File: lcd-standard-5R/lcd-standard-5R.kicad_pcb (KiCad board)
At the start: 2 copper layers, 138.2 x 93.2 mm, 56 parts, among them J1 SWD, J2 Conn_01x40_MountingPin, J3 Micro_SD_Card_Det1, J4 USB_C_Receptacle_USB2.0_16P, J5 Conn_01x06_MountingPin, SW1 BOOT0, SW2 RST, U1 siplex-som-s16, U2 TPS61169

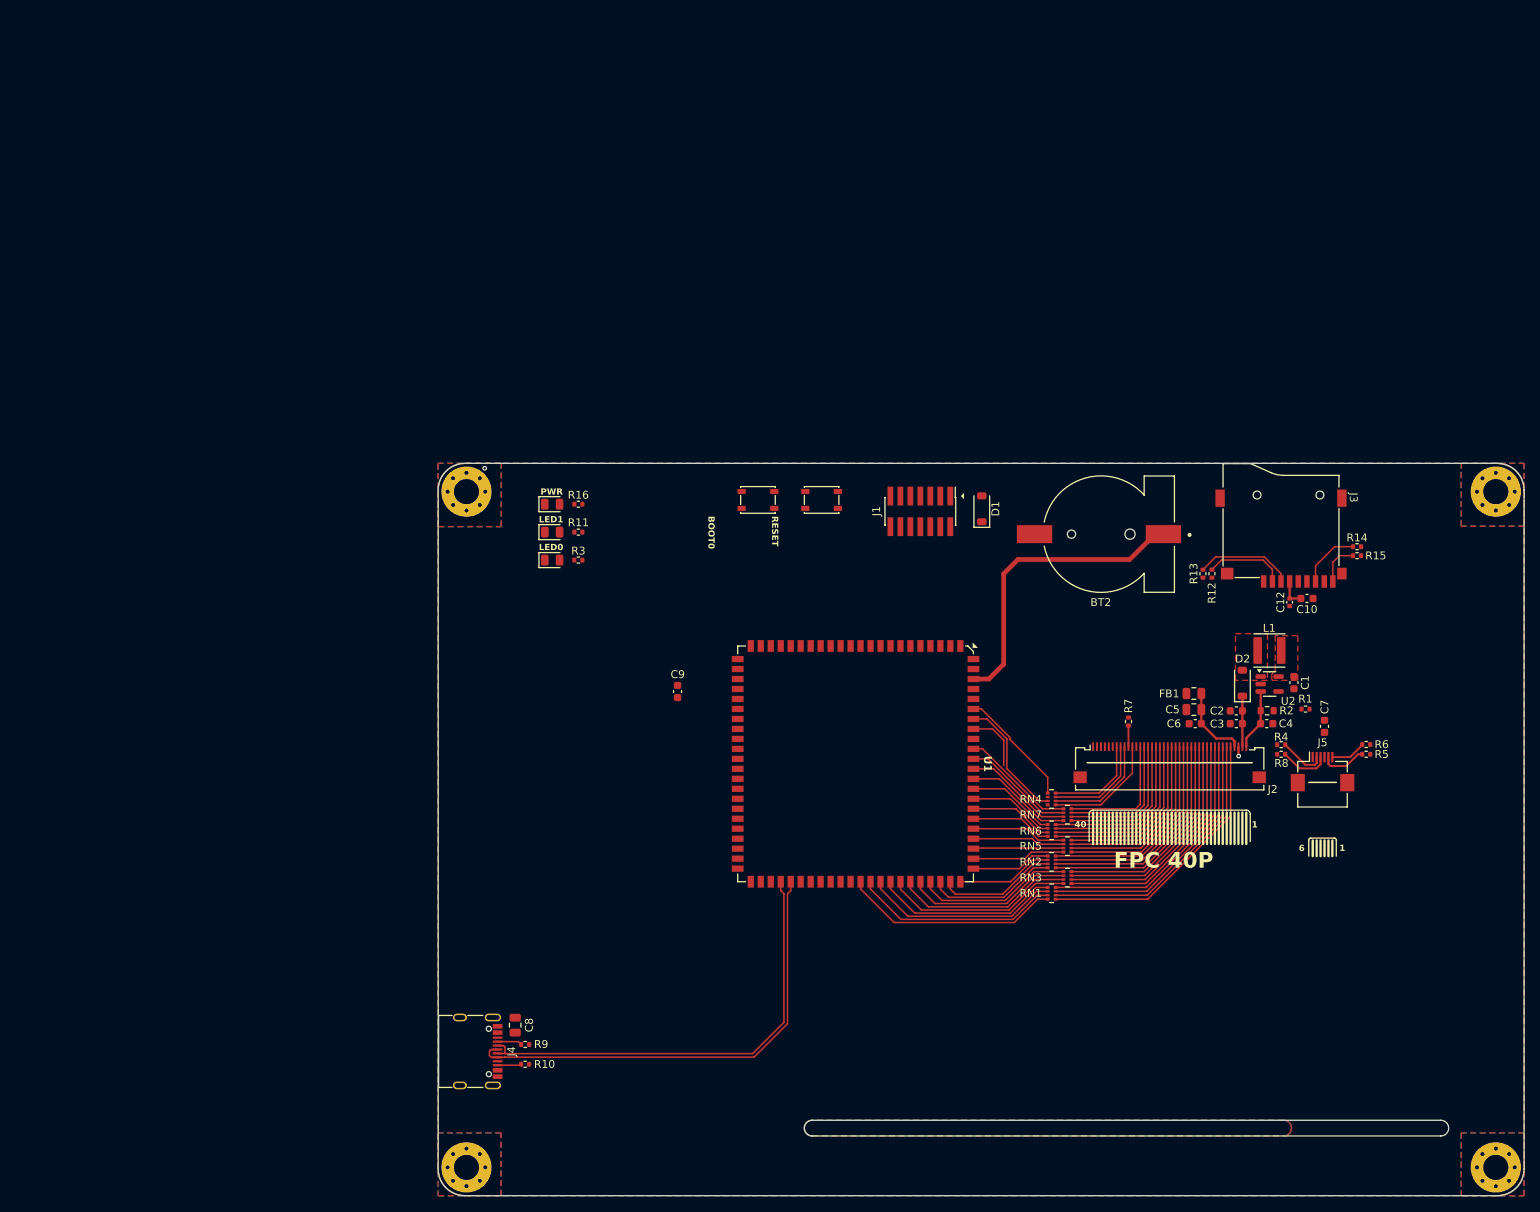
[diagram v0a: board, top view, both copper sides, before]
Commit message: Added Serial, Buzzer, AUX-IO, POWER switch, XPT2046, TAG-connect, EEPROM
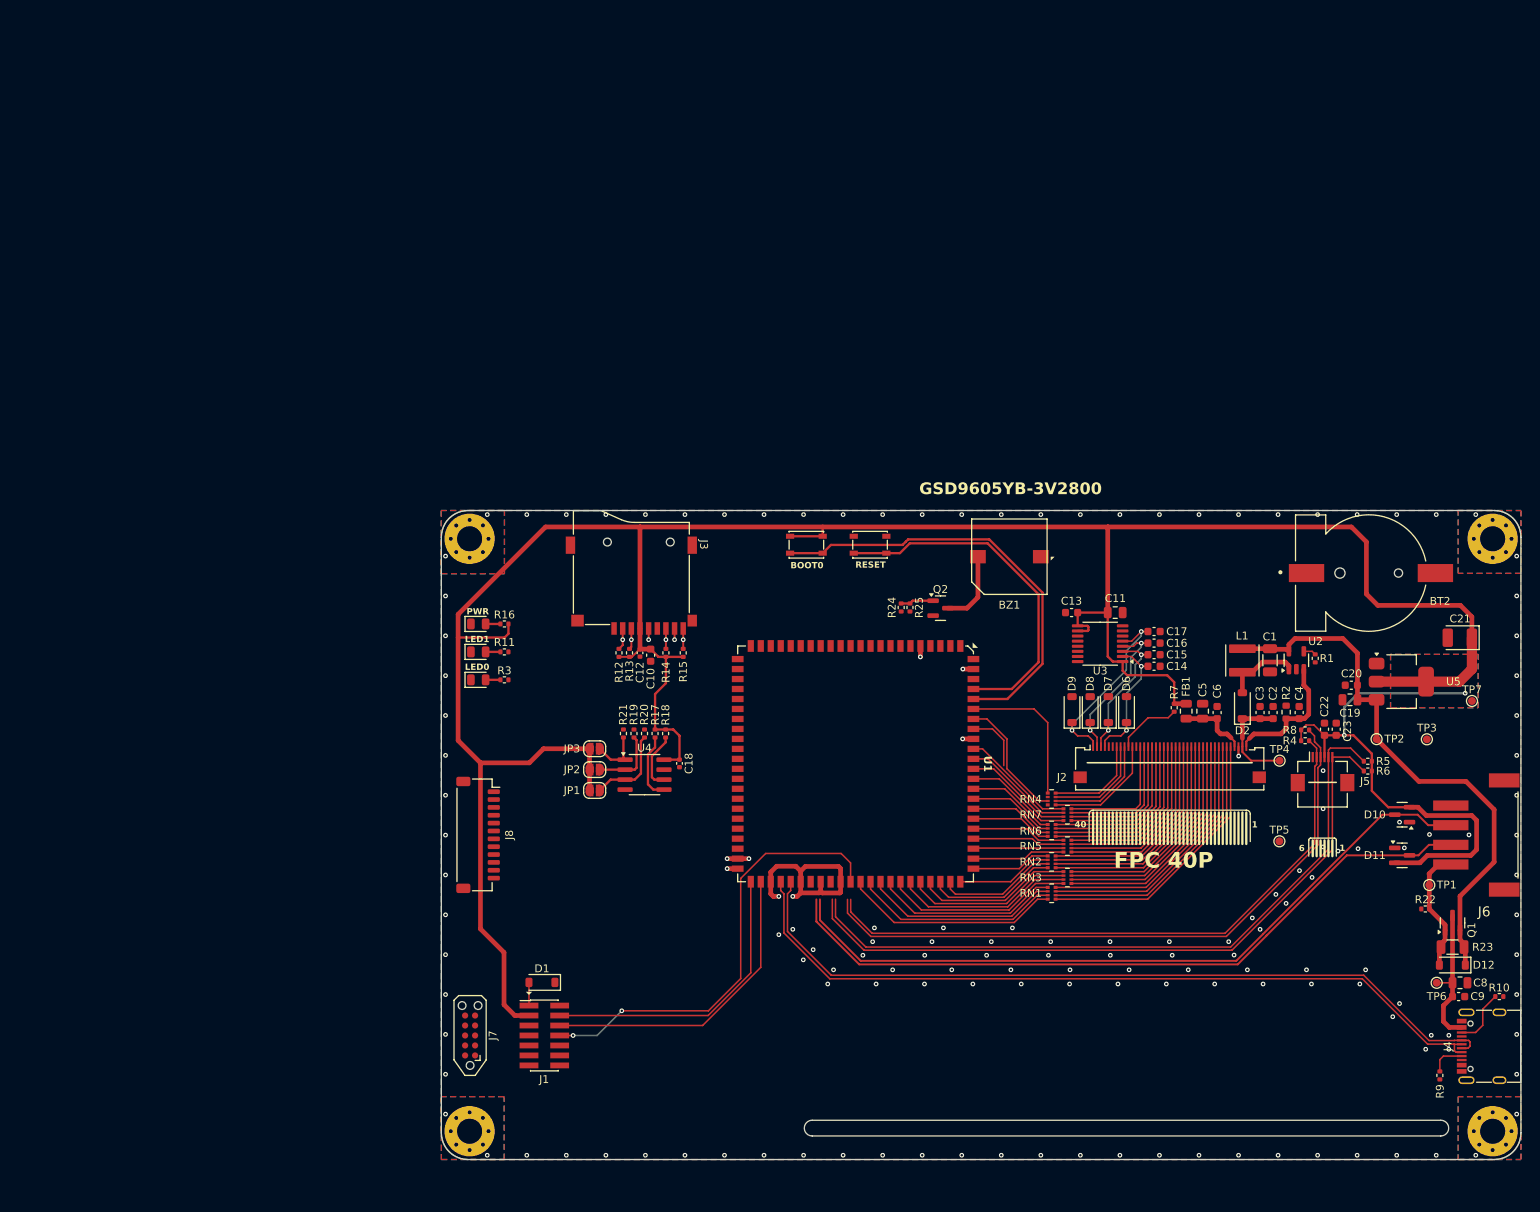
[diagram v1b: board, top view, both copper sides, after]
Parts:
- removed C7: 100n, Capacitor_SMD:C_0603_1608Metric
- removed G***: LOGO, neochrom-logo:neochrom-logo-15
- added BZ1: Buzzer, SMD-Buzzer:active-MLT-9650, F.Cu at (148.7, 59.8)
- added C11: 10u, Capacitor_SMD:C_0805_2012Metric, F.Cu at (162.2, 66.9)
- added C13: 100n, Capacitor_SMD:C_0603_1608Metric, F.Cu at (156.6, 66.9)
- added C14: 100n, Capacitor_SMD:C_0603_1608Metric, F.Cu at (167.1, 73.7)
- added C15: 100n, Capacitor_SMD:C_0603_1608Metric, F.Cu at (167.1, 72.3)
- added C16: 100n, Capacitor_SMD:C_0603_1608Metric, F.Cu at (167.1, 70.8)
- added C17: 100n, Capacitor_SMD:C_0603_1608Metric, F.Cu at (167.1, 69.3)
- added C18: 100n, Capacitor_SMD:C_0402_1005Metric, F.Cu at (106.7, 86.1)
- added C19: 10u, Capacitor_SMD:C_0805_2012Metric, F.Cu at (192.1, 78.0)
- added C20: 100n, Capacitor_SMD:C_0603_1608Metric, F.Cu at (192.2, 76.1)
- added C21: 22uF, Capacitor_Tantalum_SMD:CP_EIA-3528-12_Kemet-T, F.Cu at (206.0, 70.1)
- added C22: 1u, Capacitor_SMD:C_0603_1608Metric, F.Cu at (188.8, 81.7)
- added C23: 100n, Capacitor_SMD:C_0603_1608Metric, F.Cu at (190.3, 81.7)
- added D10: BAT54S, Package_TO_SOT_SMD:SOT-23, F.Cu at (198.7, 92.6)
- added D11: BAT54S, Package_TO_SOT_SMD:SOT-23, F.Cu at (198.7, 97.8)
- added D12: MBR0540, Diode_SMD:D_SOD-123, F.Cu at (205.1, 111.8)
- added D6: MMSZ5226BT1G, Diode_SMD:D_SOD-123, F.Cu at (163.6, 79.2)
- added D7: MMSZ5226BT1G, Diode_SMD:D_SOD-123, F.Cu at (161.3, 79.2)
- added D8: MMSZ5226BT1G, Diode_SMD:D_SOD-123, F.Cu at (159.0, 79.2)
- added D9: MMSZ5226BT1G, Diode_SMD:D_SOD-123, F.Cu at (156.7, 79.2)
- added J6: Serial, S4B-XH-SM4-TB_LF__SN:S4BXHSM4TBLFSN, F.Cu at (209.2, 95.2)
- added J7: Conn_ARM_JTAG_SWD_10, Connector:Tag-Connect_TC2050-IDC-NL_2x05_P1.27mm_Vertical, F.Cu at (80.1, 120.7)
- added J8: Conn_01x12_MountingPin, Connector_JST:JST_SH_SM12B-SRSS-TB_1x12-1MP_P1.00mm_Horizontal, F.Cu at (81.1, 95.2)
- added JP1: JMP, Jumper:SolderJumper-2_P1.3mm_Open_RoundedPad1.0x1.5mm, F.Cu at (95.9, 89.5)
- added JP2: JMP, Jumper:SolderJumper-2_P1.3mm_Open_RoundedPad1.0x1.5mm, F.Cu at (95.9, 86.9)
- added JP3: JMP, Jumper:SolderJumper-2_P1.3mm_Open_RoundedPad1.0x1.5mm, F.Cu at (95.9, 84.2)
- added Q1: DMG2301L, Package_TO_SOT_SMD:SOT-23, F.Cu at (205.1, 106.4)
- added Q2: MMBT3904, Package_TO_SOT_SMD:SOT-23, F.Cu at (140.0, 66.3)
- added R17: 2K2, Resistor_SMD:R_0402_1005Metric, F.Cu at (103.6, 82.3)
- added R18: 2K2, Resistor_SMD:R_0402_1005Metric, F.Cu at (105.0, 82.3)
- added R19: 2K2, Resistor_SMD:R_0402_1005Metric, F.Cu at (100.9, 82.3)
- added R20: 2K2, Resistor_SMD:R_0402_1005Metric, F.Cu at (102.3, 82.3)
- added R21: 2K2, Resistor_SMD:R_0402_1005Metric, F.Cu at (99.6, 82.3)
- added R22: 10K, Resistor_SMD:R_0402_1005Metric, F.Cu at (201.7, 104.6)
- added R23: 0, Resistor_SMD:R_1206_3216Metric, F.Cu at (205.1, 109.5)
- added R24: 1K, Resistor_SMD:R_0402_1005Metric, F.Cu at (135.0, 66.3)
- added R25: 10K, Resistor_SMD:R_0402_1005Metric, F.Cu at (136.1, 66.3)
- added TP1: TestPoint, TestPoint:TestPoint_Pad_D1.0mm, F.Cu at (202.2, 101.6)
- added TP2: TestPoint, TestPoint:TestPoint_Pad_D1.0mm, F.Cu at (195.5, 83.0)
- added TP3: TestPoint, TestPoint:TestPoint_Pad_D1.0mm, F.Cu at (201.9, 83.0)
- added TP4: TestPoint, TestPoint:TestPoint_Pad_D1.0mm, F.Cu at (183.1, 85.8)
- added TP5: TestPoint, TestPoint:TestPoint_Pad_D1.0mm, F.Cu at (183.1, 96.0)
- added TP6: TestPoint, TestPoint:TestPoint_Pad_D1.0mm, F.Cu at (203.1, 114.0)
- added TP7: TestPoint, TestPoint:TestPoint_Pad_D1.0mm, F.Cu at (207.6, 78.2)
- added U3: XPT2046TS, Package_SO:TSSOP-16_4.4x5mm_P0.65mm, F.Cu at (160.3, 70.9)
- added U4: CAT24C256, Package_SO:SOIC-8_3.9x4.9mm_P1.27mm, F.Cu at (102.3, 87.5)
- added U5: AMS1117-3.3, Package_TO_SOT_SMD:SOT-223-3_TabPin2, F.Cu at (198.6, 75.7)
- C1: footprint Capacitor_SMD:C_0603_1608Metric -> Capacitor_SMD:C_1206_3216Metric
- moved J4 130.1 mm to (210.0, 122.1), turned to 90 degrees
- moved R10 124.3 mm to (211.1, 115.8)
- moved C8 120.4 mm to (206.1, 114.0), turned to 0 degrees
- moved R9 116.5 mm to (203.5, 125.8), turned to 90 degrees
- moved C9 106.7 mm to (205.9, 115.8), turned to 0 degrees
- moved R14 89.0 mm to (105.0, 72.0), turned to 90 degrees
- moved R15 86.6 mm to (107.2, 72.0), turned to 90 degrees
- moved C10 83.8 mm to (103.1, 72.3), turned to -90 degrees
- moved C12 82.9 mm to (101.7, 72.0)
- moved J3 82.9 mm to (100.6, 63.7)
- moved D1 82.3 mm to (89.2, 114.0), turned to 180 degrees
- moved J1 82.1 mm to (89.5, 120.7), turned to 0 degrees
- moved R12 76.1 mm to (99.0, 72.0)
- moved R13 73.7 mm to (100.4, 72.0)
- moved BT2 34.5 mm to (194.5, 61.9), turned to -90 degrees
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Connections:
- C1 pad 1: +5V -> VDD
- D1 pad 1: +5V -> VDD
- L1 pad 1: +5V -> VDD
- R1 pad 1: +5V -> /LCD_BLK
- R1 pad 2: /LCD_BLK -> GND
- U1 pad 41: VBUS -> VDD
- U2 pad 5: +5V -> VDD
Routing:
- net +3V3: track 3.59 -> 402.8 mm, vias 0 -> 2
- net /SERIAL_RX: track 0.00 -> 93.3 mm
- net /SERIAL_TX: track 0.00 -> 92.1 mm
- net /TP_SCL: track 4.51 -> 89.6 mm
- net /TP_SDA: track 5.90 -> 89.7 mm
- net /TP_WAKE: track 6.37 -> 83.0 mm
- net /TP_INT: track 5.92 -> 80.1 mm
- net VDD: track 0.00 -> 70.7 mm
- net /SWO: track 0.00 -> 57.0 mm, vias 0 -> 2
- net /BOOT0: track 0.00 -> 55.4 mm
- net /RESET: track 0.00 -> 45.1 mm
- net /USB_DN: track 58.0 -> 100.6 mm
- net /USB_DP: track 59.7 -> 100.9 mm
- net /SWCLK: track 0.00 -> 39.6 mm
- net VBAT: track 38.6 -> 0.00 mm
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- added copper zone on B.Cu, net +3V3
- added copper zone on F.Cu, net +3V3
- removed copper zone on F.Cu, net +5V
- removed copper zone on F.Cu, net /SW
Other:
- board size 138.2 x 93.2 mm -> 137.4 x 82.6 mm
- board text added: "AUX - IO"
- board text added: "GSD9605YB-3V2800"
- board text added: "SERIAL"
- board text added: "ST-LINK"
- board text added: "USB"
- board text added: "uSD"

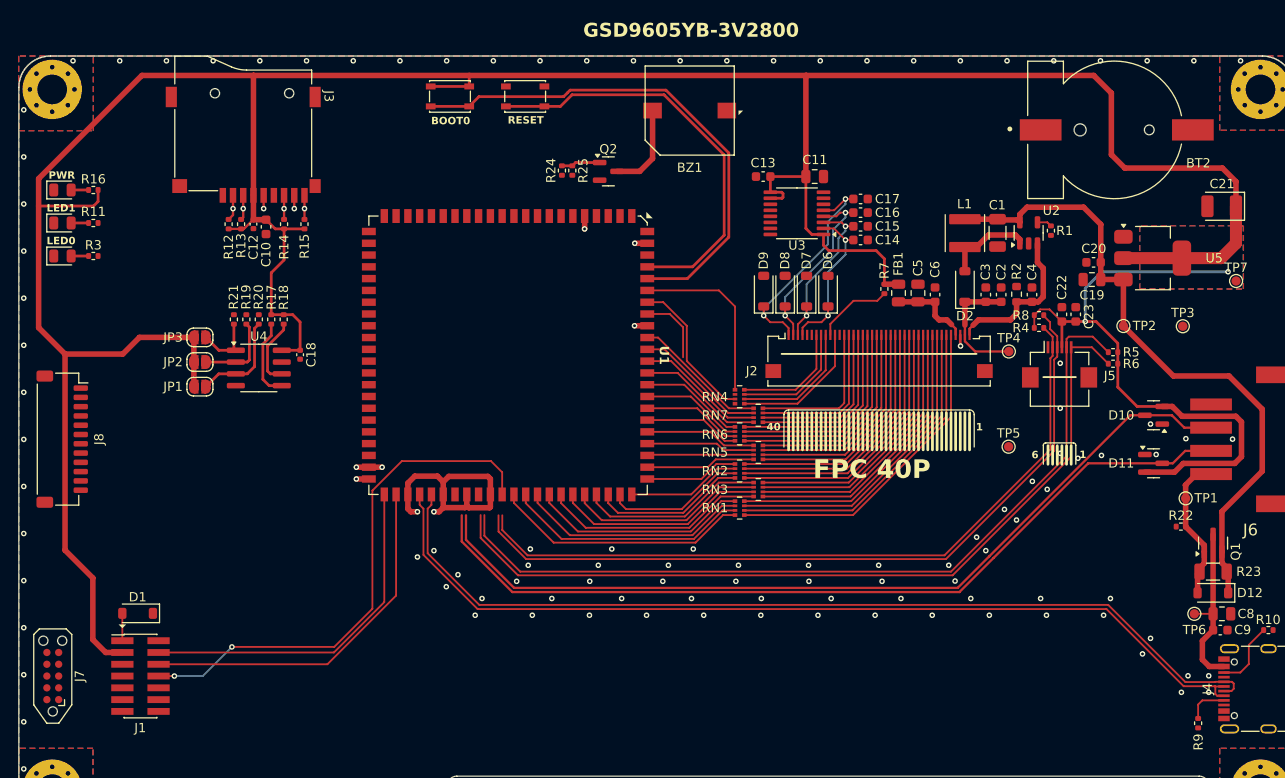
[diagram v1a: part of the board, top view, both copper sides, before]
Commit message: LCD 5 inch, Finished SD card, Touch, Buzzer etc, LCD Bar 3.4, Adding resistor on st-link, not finished yet
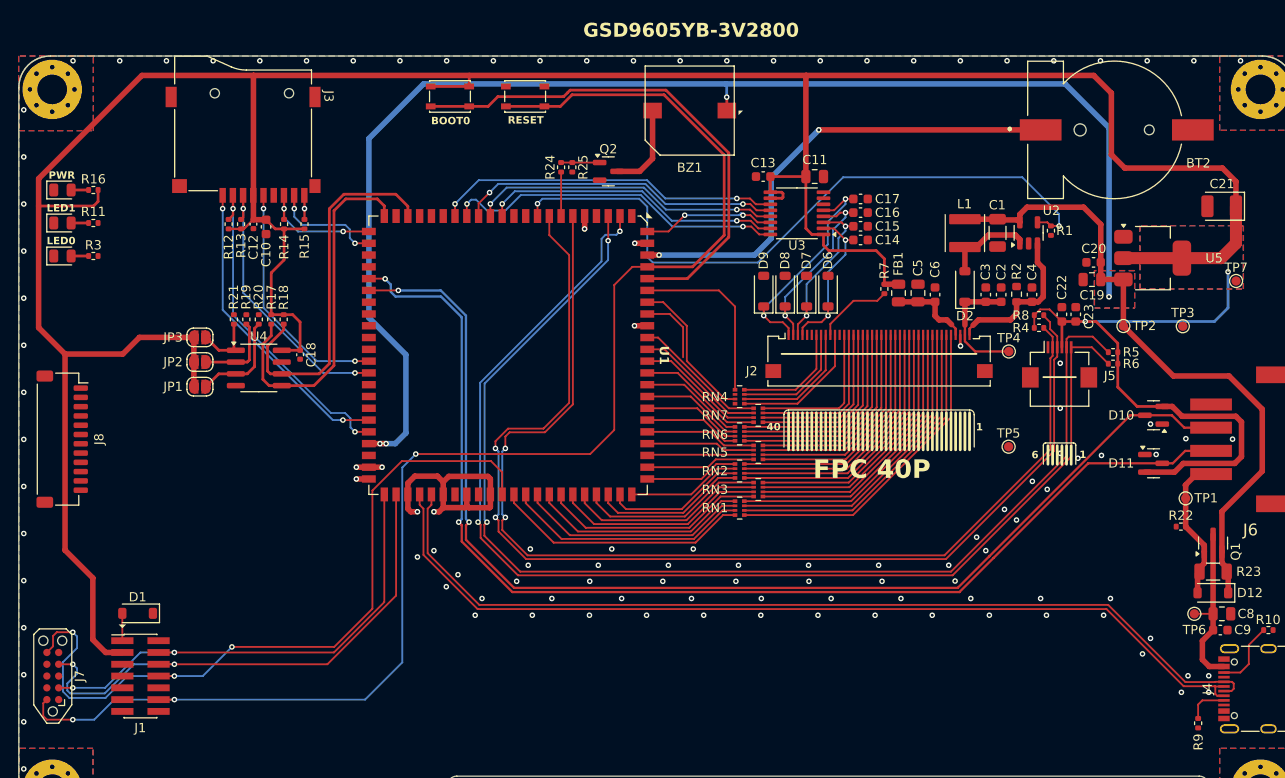
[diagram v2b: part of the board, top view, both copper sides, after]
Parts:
- BZ1: value Buzzer -> MLT-9650
- moved R24 0.36 mm to (134.9, 65.9)
- moved R25 0.35 mm to (136.1, 65.9)
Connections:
- R17 pad 2: Net-(U4-SDA) -> /EE_SDA
- R18 pad 2: Net-(U4-SCL) -> /EE_SCL
- U1 pad 1: /LCD_RST -> unconnected-(U1-PB7-Pad1)
- U1 pad 12: unconnected-(U1-PA3-Pad12) -> /TP_CS
- U1 pad 13: unconnected-(U1-PA7-Pad13) -> /TP_BUSY
- U1 pad 14: unconnected-(U1-PA6-Pad14) -> /TP_MISO
- U1 pad 15: unconnected-(U1-PA5-Pad15) -> /TP_CLK
- U1 pad 16: unconnected-(U1-PB0-Pad16) -> /TP_IRQ
- U1 pad 2: /LCD_TP_SCL -> /TP_SCL
- U1 pad 20: unconnected-(U1-PB10-Pad20) -> /EE_SCL
- U1 pad 22: unconnected-(U1-PB11-Pad22) -> /EE_SDA
- U1 pad 23: unconnected-(U1-PB14-Pad23) -> /DAT0
- U1 pad 24: unconnected-(U1-PB15-Pad24) -> /DAT1
- U1 pad 27: unconnected-(U1-PC6-Pad27) -> /SERIAL_TX
- U1 pad 28: unconnected-(U1-PC7-Pad28) -> /SERIAL_RX
- U1 pad 3: /LCD_TP_SDA -> /TP_SDA
- U1 pad 34: unconnected-(U1-PD6-Pad34) -> /CLK
- U1 pad 35: unconnected-(U1-PD7-Pad35) -> /CMD
- U1 pad 39: /LCD_SPI_CLK -> /DAT2
- U1 pad 4: /LCD_TP_INT -> unconnected-(U1-PH4-Pad4)
- U1 pad 40: /LCD_SPI_CS -> /DAT3
- U1 pad 6: /LCD_TP_RST -> /TP_INT
- U1 pad 7: unconnected-(U1-PC1-Pad7) -> /BUZZER
- U1 pad 8: unconnected-(U1-PC4-Pad8) -> /TP_WAKE
- U1 pad 88: /LCD_SPI_DAT -> /TP_MOSI
- U1 pad 9: unconnected-(U1-PA0-Pad9) -> /LCD_BLK
- U4 pad 5: Net-(U4-SDA) -> /EE_SDA
- U4 pad 6: Net-(U4-SCL) -> /EE_SCL
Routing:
- net VDD: track 70.7 -> 214.5 mm, vias 0 -> 4
- net /RESET: track 45.1 -> 155.6 mm, vias 0 -> 3
- net /LCD_BLK: track 1.61 -> 73.0 mm, vias 0 -> 2
- net VBAT: track 0.00 -> 51.8 mm, vias 0 -> 2
- net /EE_SCL: track 0.00 -> 40.4 mm
- net /TP_SCL: track 89.6 -> 129.0 mm, vias 0 -> 2
- net /EE_SDA: track 0.00 -> 39.2 mm
- net /TP_WAKE: track 83.0 -> 122.1 mm, vias 0 -> 2
- net /TP_SDA: track 89.7 -> 127.6 mm, vias 0 -> 2
- net /TP_INT: track 80.1 -> 118.0 mm, vias 0 -> 2
- net /TP_IRQ: track 0.00 -> 37.4 mm, vias 0 -> 2
- net /TP_CLK: track 0.00 -> 37.1 mm, vias 0 -> 2
- net /TP_MISO: track 0.00 -> 34.8 mm, vias 0 -> 2
- net /SERIAL_TX: track 92.1 -> 125.9 mm, vias 0 -> 2
- net /TP_BUSY: track 0.00 -> 33.5 mm, vias 0 -> 2
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- added copper zone on B.Cu, net VDD
- added copper zone on F.Cu, net VDD
